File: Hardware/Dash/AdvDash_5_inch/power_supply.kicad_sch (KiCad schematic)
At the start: 50 parts, among them Q1 BSS139H6327XTSA1, T1 IRFR5305, U1 TPS54331DDA, U8 LD1086DT33TR

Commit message: PCB R0.1.0
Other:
- company: (none) -> ADV.ECU - GNVPerformance
- title: (none) -> Power Supply 3.3v - 5v / 3.3v Always ON

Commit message: :adhesive_bandage: Minor change to the PCB
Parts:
- C1, C5: LCSC (none) -> C1872
- C10: LCSC (none) -> C531418
- C11: LCSC (none) -> C83170
- C13: LCSC (none) -> C2992591
- C14: LCSC (none) -> C116352
- C18, C2: LCSC (none) -> C38141
- C28, C29: LCSC (none) -> C1713
- C3: LCSC (none) -> C1817
- C4: LCSC (none) -> C106239
- C7: LCSC (none) -> C342606
- C8: LCSC (none) -> C1744
- D12: LCSC (none) -> C965819
- D2: LCSC (none) -> C437199
- D3: LCSC (none) -> C64982
- D3, D4: LCSC (none) -> C965818
- D5: LCSC (none) -> C151257
- D6: LCSC (none) -> C965812
- F1: LCSC C883140 -> C883154
- F2: LCSC (none) -> C883154
- G1: Manufacturer_Part_Number (none) -> 726-TLF80511TFV33AT2
- L1: LCSC (none) -> C2847472
- Q1: LCSC (none) -> C2998039
- R12: LCSC (none) -> C2933303
- R12: value 10k -> 10K; LCSC (none) -> C17414
- R12: LCSC (none) -> C17604
- R2: LCSC (none) -> C5266070
- R3: LCSC (none) -> C2999452
- R3: LCSC (none) -> C2907449
- R4: LCSC (none) -> C17719
- R5: value 332 -> 332k; LCSC (none) -> C17632
- R7: value 0 -> 0R; LCSC (none) -> C17477
- U1: LCSC (none) -> C90761
- U8: LCSC (none) -> C12051

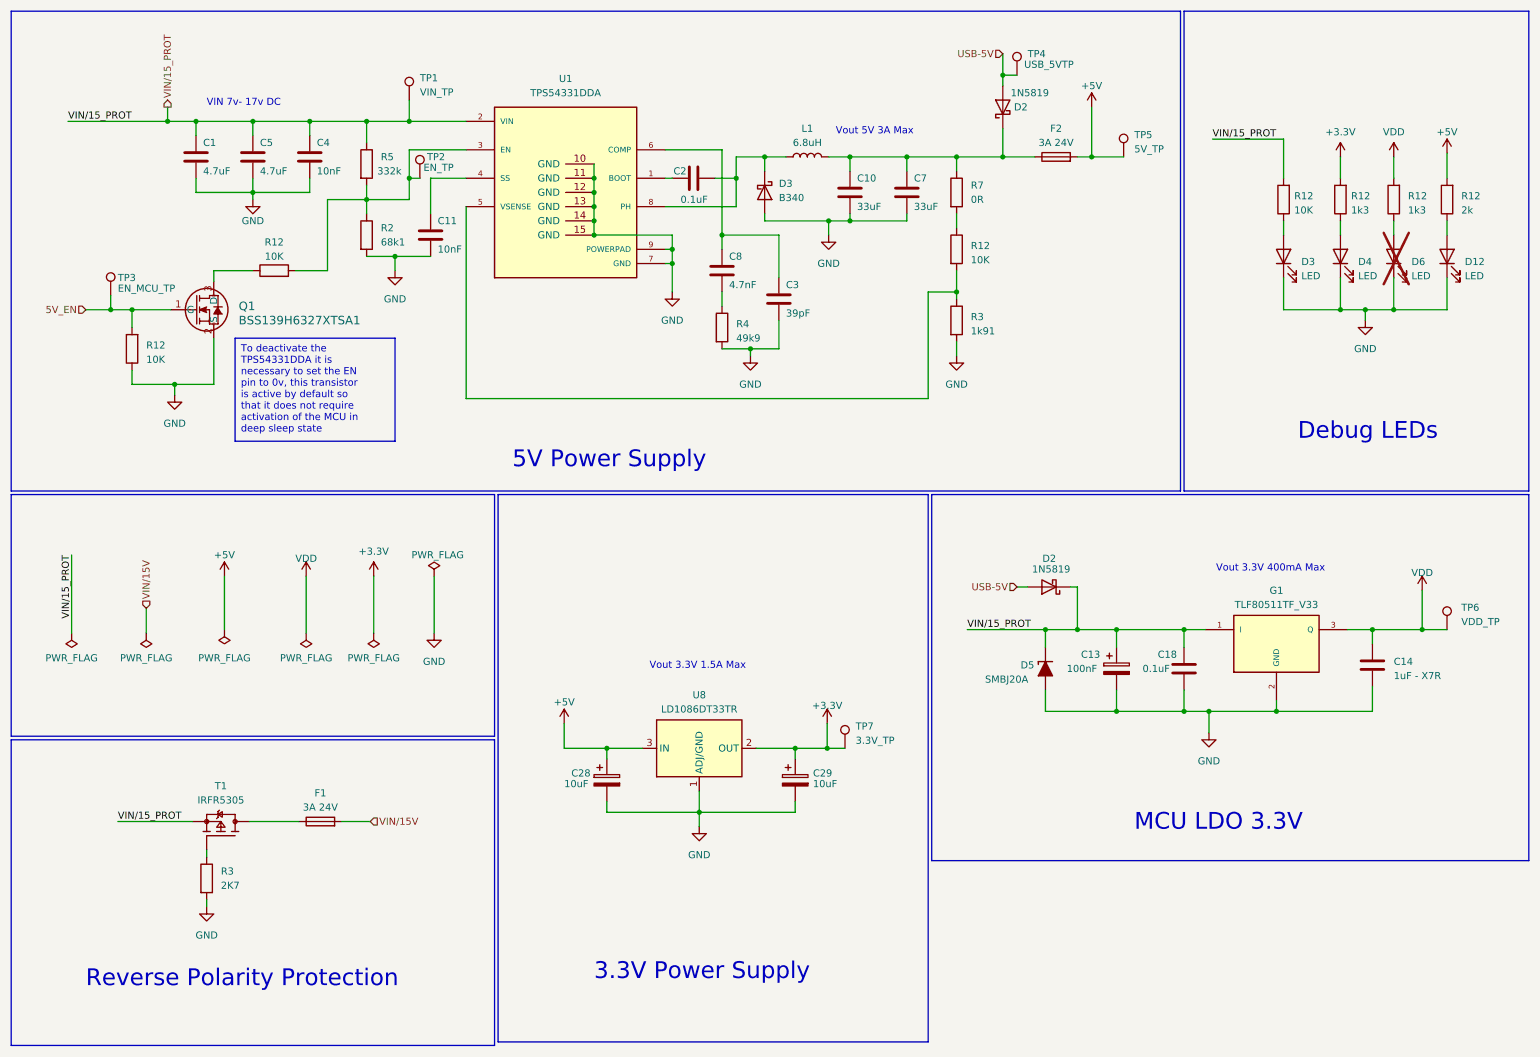
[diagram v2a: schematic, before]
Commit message: :adhesive_bandage: Fix errors in pcb desing, changelog in file, rev0.2.0
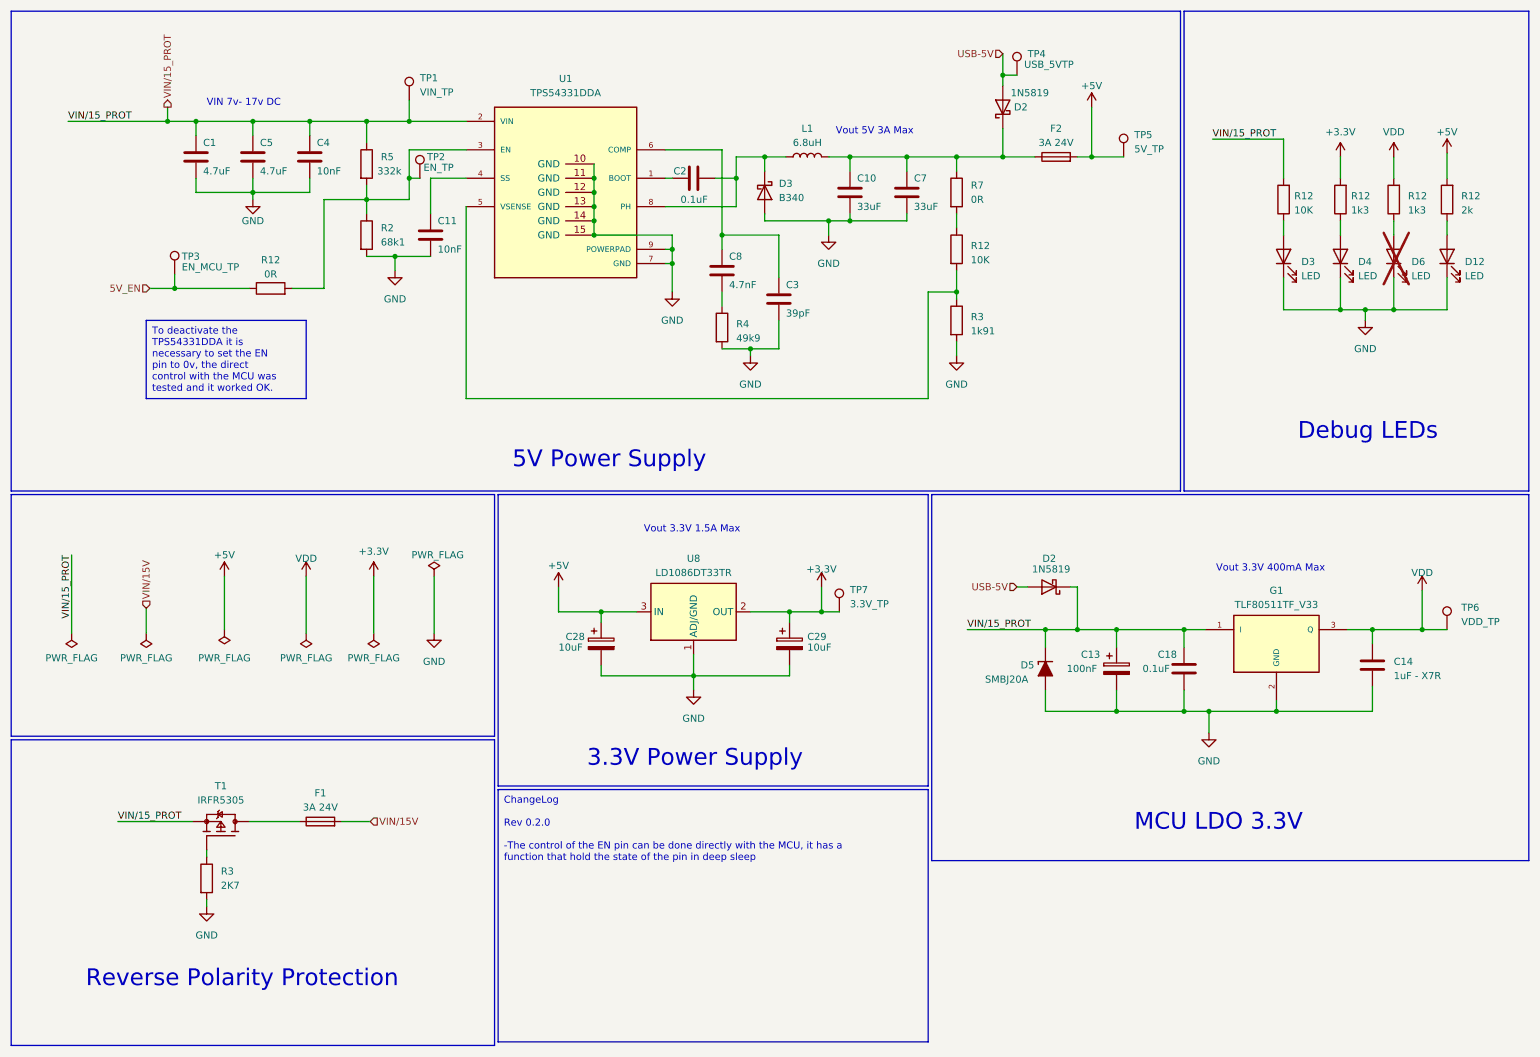
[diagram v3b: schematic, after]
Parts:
- removed Q1: BSS139H6327XTSA1, PCM_Package_TO_SOT_SMD_AKL:SOT-23, symbol 2023-10-22_21-56-23:BSS139H6327XTSA1
- removed R12: 10K, Resistor_SMD:R_0805_2012Metric_Pad1.20x1.40mm_HandSolder, symbol Device:R
- R12: value 10K -> 0R
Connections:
- net 5V_EN: now also R12.1
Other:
- moved on the sheet: C28, C29, R12, TP3, TP7, U8

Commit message: :bug: PCB R0.2.0 Ready, change log in kicad files
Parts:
- R5: LCSC C17632 -> C212383; LCSC Part Number C17632 -> C212383
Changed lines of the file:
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@@
     )
   )
-  (text_box "ChangeLog\n\nRev 0.2.0\n\n-The control of the EN pin can be done directly with the MCU, it has a function that hold the state of the pin in deep sleep"
+  (text_box "ChangeLog\n\nRev 0.2.0\n\n-The control of the EN pin can be done directly with the MCU, it has a function that hold the state of the pin in deep sleep\n\n-R3 Part number fix"
     (at 99.695 152.4 0) (size 76.835 45.085)
     (stroke (width 0) (type default))
@@
       (effects (font (size 1.27 1.27)) hide)
     )
-    (property "LCSC Part Number" "C17632" (at 76.2 40.64 0)
-      (effects (font (size 1.27 1.27)) hide)
-    )
-    (property "LCSC" "C17632" (at 76.2 40.64 0)
-      (effects (font (size 1.27 1.27)) hide)
-    )
-    (pin "1")
+    (property "LCSC Part Number" "C212383" (at 76.2 40.64 0)
+      (effects (font (size 1.27 1.27)) hide)
+    )
+    (property "LCSC" "C212383" (at 76.2 40.64 0)
+      (effects (font (size 1.27 1.27)) hide)
+    )
+    (property "MOUSER" "" (at 76.2 40.64 0)
+      (effects (font (size 1.27 1.27)))
+    )
+    (pin "1")
